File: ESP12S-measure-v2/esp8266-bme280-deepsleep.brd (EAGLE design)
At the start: 40.6 x 87.9 mm, 21 parts, among them U1 74HC4051D,653

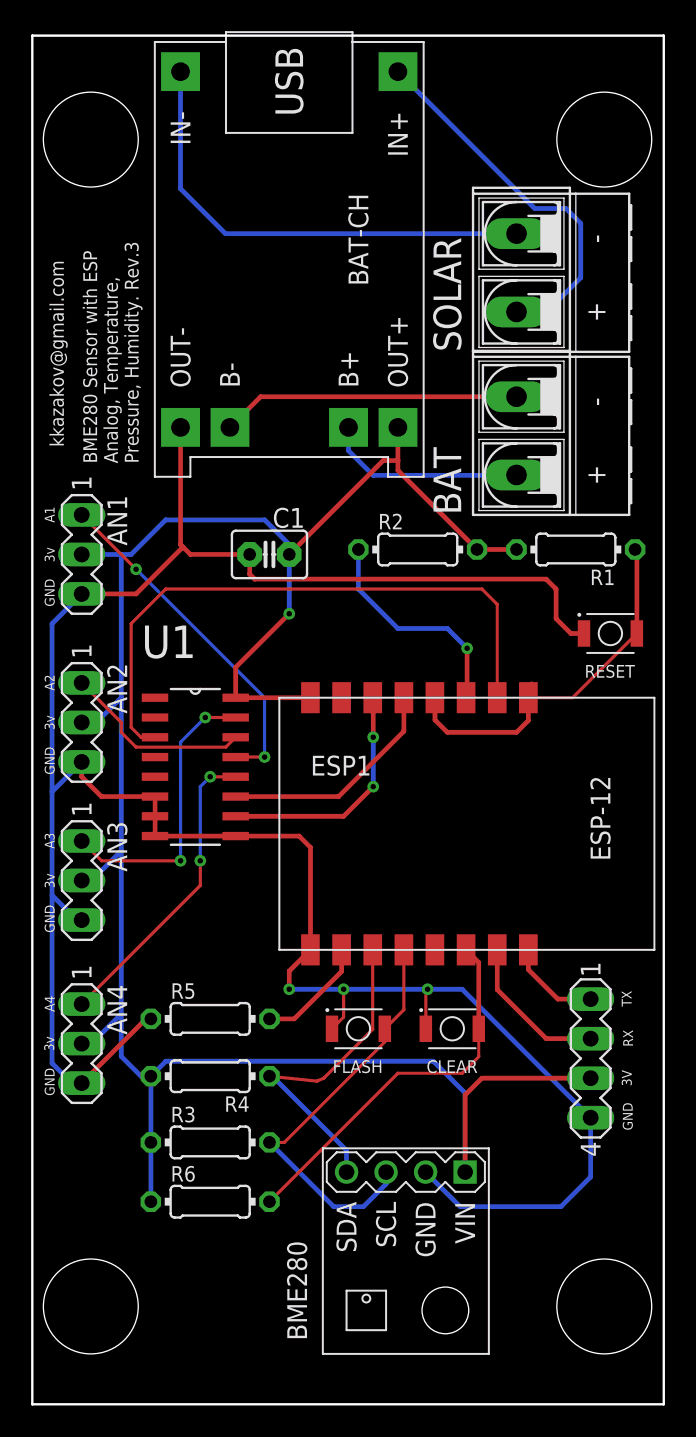
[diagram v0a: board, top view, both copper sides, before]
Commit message: The board now goes to deep sleep and not in soft ap, if the ssid cannot be found. This is crucial, so that it does not drain the battery.
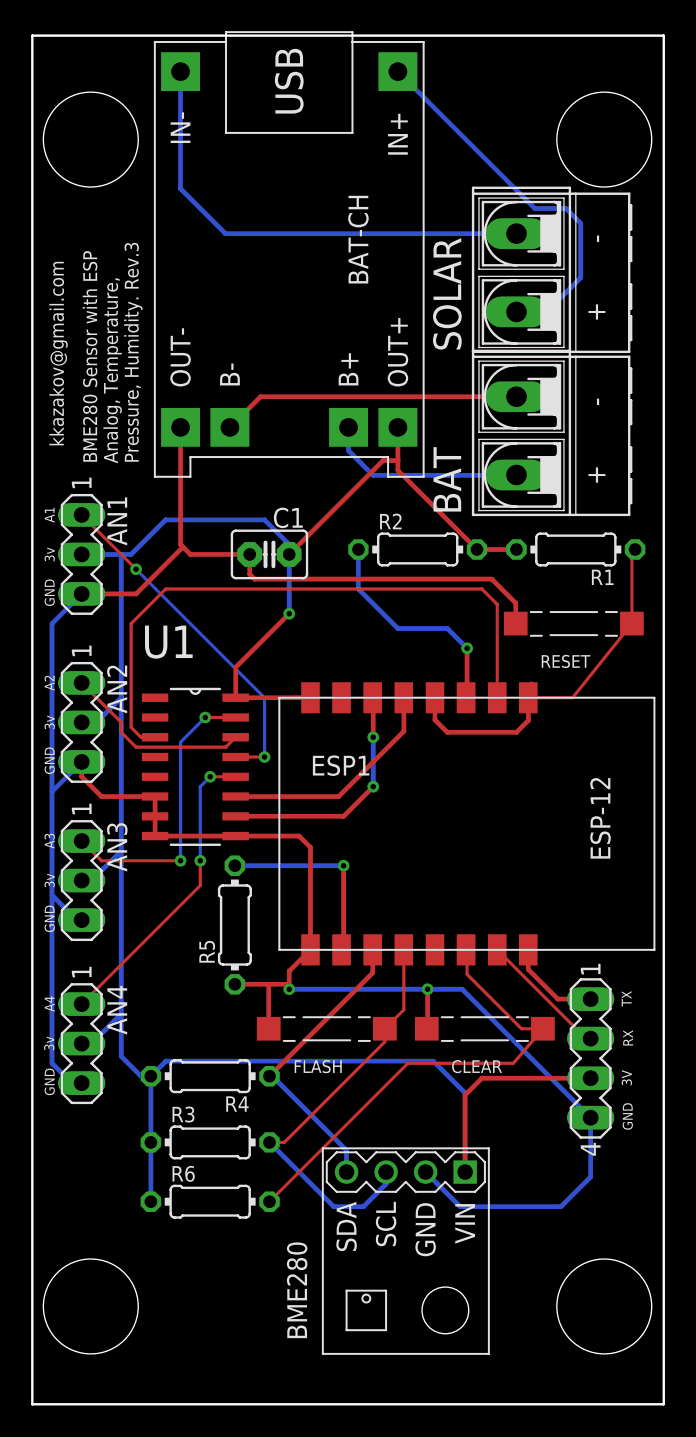
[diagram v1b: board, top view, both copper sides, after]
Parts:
- CLEAR, FLASH, RESET: value B3U-1000P -> SWCH-SMD-1; device B3U-1000P:SW_B3U-1000P -> SMD-SWITCH-1:SWCH-SMD-1
- moved R5 6.24 mm to (24.4, 25.4), turned to 90 degrees
- moved RESET 2.93 mm to (45.7, 44.8)
- moved FLASH 2.54 mm to (29.8, 18.7)
- moved CLEAR 1.59 mm to (40.0, 18.7)
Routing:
- net GND: track 164.0 -> 156.4 mm, vias 3 -> 2
- net CLEAR: track 24.5 -> 30.2 mm
- net N$8: track 7.29 -> 12.4 mm, vias 0 -> 1
- net SDA: track 21.4 -> 19.2 mm
- net RX: track 9.87 -> 8.37 mm
